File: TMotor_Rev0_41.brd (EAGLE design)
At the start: 106.7 x 79.4 mm, 105 parts, among them U1 INA125U, U10 DEV-16771, U2 INA125U, U3 INA125U, U4 INA125U, U5 SN65HVD230MDREP, U6 2SJ305TE85LF, U7 2SJ305TE85LF, U8 2SJ305TE85LF, U9 2SJ305TE85LF

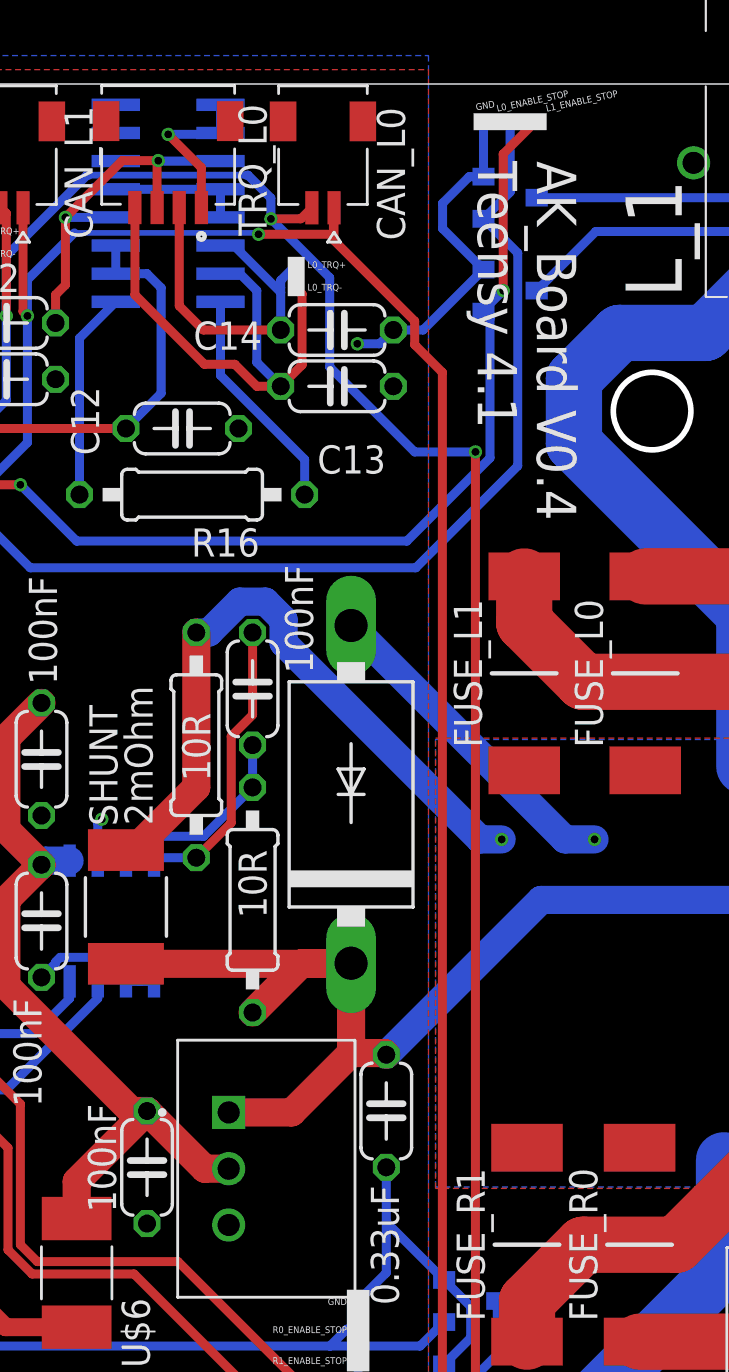
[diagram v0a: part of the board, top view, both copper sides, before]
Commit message: fixed 5v regulator in rev 0.41
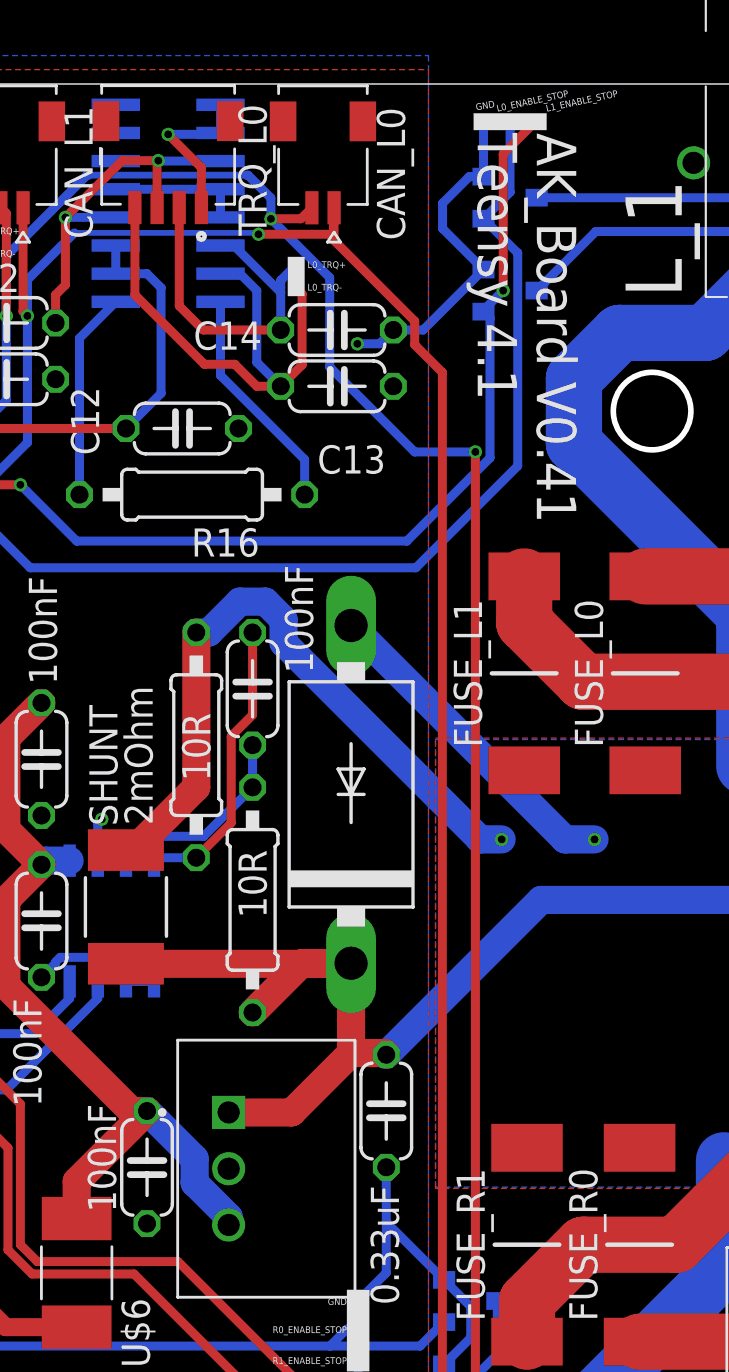
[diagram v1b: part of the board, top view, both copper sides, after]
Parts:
- U$11: device SnapEDA-Library:P78E05-1000 -> SnapEDA-Library_Paul:P78E05-1000
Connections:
- net GND: now also U$11.2; no longer U$11.3
- net VIN: now also U$11.3; no longer U$11.2
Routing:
- net VIN: track 35.7 -> 37.6 mm
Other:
- board text added: "AK_Board V0.41 Teensy 4.1"
- board text removed: "AK_Board V0.4 Teensy 4.1"
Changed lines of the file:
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@@
 <circle x="42.475" y="69.365" radius="1.75" width="0.254" layer="20"/>
 <circle x="42.475" y="21.365" radius="1.75" width="0.254" layer="20"/>
-<text x="34.6075" y="80.645" size="1.778" layer="21" rot="SR270">AK_Board V0.4
+<text x="34.6075" y="81.915" size="1.778" layer="21" rot="SR270">AK_Board V0.41
 Teensy 4.1</text>
 <text x="-33.147" y="62.23" size="1.778" layer="121">+</text>
@@
 </polygon>
 <polygon width="0.1524" layer="41">
-<vertex x="29.21" y="12.7"/>
-</polygon>
-<polygon width="0.1524" layer="41">
 <vertex x="23.114" y="22.86"/>
 <vertex x="23.368" y="22.86"/>
@@
 <polygon width="0.1524" layer="41">
 <vertex x="25.4" y="73.66"/>
-<vertex x="25.019" y="74.041"/>
 <vertex x="25.019" y="74.041"/>
 </polygon>
@@
 <attribute name="VALUE" x="56.769" y="17.653" size="1.778" layer="27" ratio="10" rot="R180"/>
 </element>
-<element name="U$11" library="SnapEDA-Library" package="P78E05-1000" value="P78E05-1000" x="25.908" y="35.179" smashed="yes" rot="R270">
+<element name="U$11" library="SnapEDA-Library_Paul" package="P78E05-1000" value="P78E05-1000" x="25.908" y="35.179" smashed="yes" rot="R270">
 <attribute name="VALUE" x="20.216" y="41.093" size="1.27" layer="27"/>
 </element>
@@
 <contactref element="U$3" pad="2"/>
 <contactref element="U$4" pad="2"/>
-<contactref element="U$11" pad="3"/>
+<contactref element="U$11" pad="2"/>
 <wire x1="48.7823" y1="10.7711" x2="46.5477" y2="10.7711" width="2.54" layer="16"/>
 <wire x1="45.72" y1="30.69886875" x2="45.72" y2="35.56" width="2.54" layer="16"/>
@@
 <wire x1="16.51" y1="34.6075" x2="19.685" y2="37.7825" width="1.27" layer="1"/>
 <wire x1="18.9793375" y1="37.7825" x2="19.685" y2="37.7825" width="1.27" layer="1"/>
-<contactref element="U$11" pad="2"/>
-<wire x1="19.685" y1="37.7825" x2="22.2885" y2="35.179" width="1.27" layer="1"/>
-<wire x1="22.2885" y1="35.179" x2="23.368" y2="35.179" width="1.27" layer="1"/>
+<contactref element="U$11" pad="3"/>
+<wire x1="19.685" y1="37.7825" x2="21.8306" y2="35.6369" width="1.27" layer="16"/>
+<wire x1="21.8306" y1="35.6369" x2="21.8306" y2="34.5421875" width="1.27" layer="16"/>
+<wire x1="23.368" y1="33.0047875" x2="23.368" y2="32.639" width="1.27" layer="16"/>
+<wire x1="21.8306" y1="34.5421875" x2="23.368" y2="33.0047875" width="1.27" layer="16"/>
 </signal>
 <signal name="3.3V">
